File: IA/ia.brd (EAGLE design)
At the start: 90 x 60 mm, 20 parts, among them IC1 7805TV

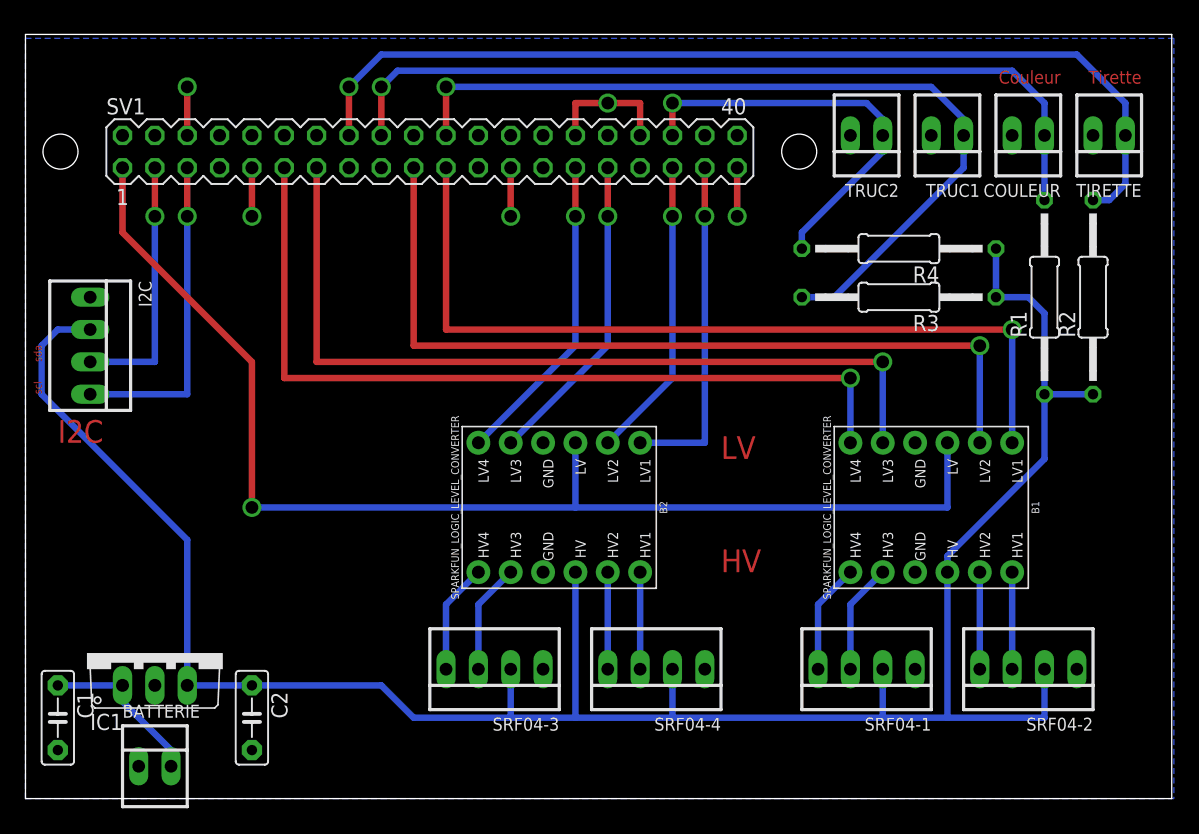
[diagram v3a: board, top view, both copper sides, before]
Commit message: puissance IA + carte AX12
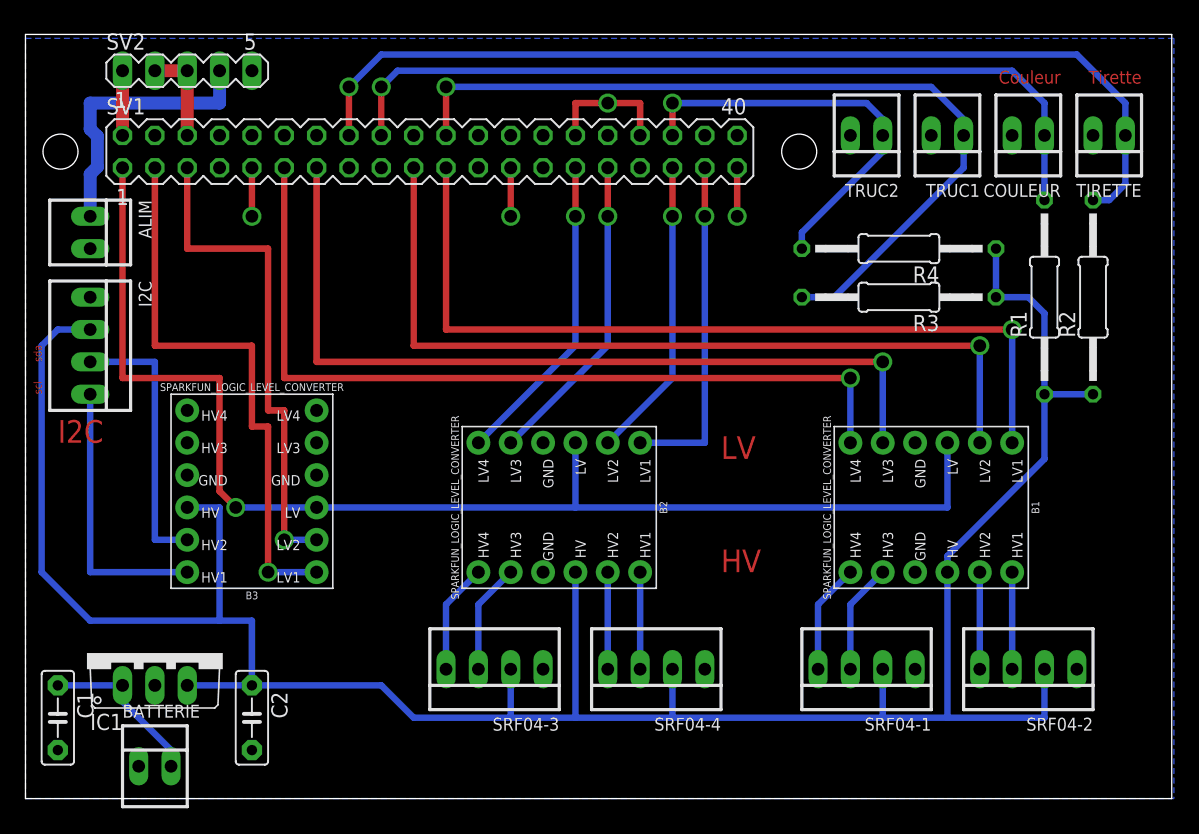
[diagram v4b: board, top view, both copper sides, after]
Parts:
- added ALIM: 22-23-2021, con-molex:22-23-2021
- added B3: SPARKFUN_LOGIC_LEVEL_CONVERTER, SparkFun-Boards:SPARKFUN_LOGIC_LEVEL_CONVERTER
- added SV2: (no value), con-lstb:MA05-1
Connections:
- new net N$10: B3.HV2, I2C.3
- new net N$11: B3.HV1, I2C.4
- new net N$13: SV1.2, SV2.1
- new net N$14: ALIM.1, SV2.4
- net GND: now also ALIM.2, B3.GND1, B3.GND2, SV2.2, SV2.3
- net SCL: now also B3.LV2; no longer I2C.4
- net SDA: now also B3.LV1; no longer I2C.3
- net VCC: now also B3.HV
- net VCC_1: now also B3.LV
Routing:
- net SDA: track 20.3 -> 44.5 mm
- net N$14: track 0.00 -> 22.1 mm
- net N$11: track 0.00 -> 21.6 mm
- net N$10: track 0.00 -> 21.6 mm
- net VCC: track 177.6 -> 198.6 mm
- net SCL: track 25.4 -> 39.4 mm
- net VCC_1: track 95.6 -> 100.9 mm
- net N$13: track 0.00 -> 5.08 mm
- net GND: track 25.4 -> 29.2 mm, vias 5 -> 4
